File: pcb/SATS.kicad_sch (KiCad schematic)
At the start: 27 parts, among them J1 Raspberry_Pi_2_3, J10 EXT_GPIO, J11 EXT_GPIO, J12 EXT_GPIO, J13 EXT_GPIO, J2 A00-432-262-450, J3 AudioJack4_SwitchTR1, J4 5V, J5 3.3V, J6 Card LED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

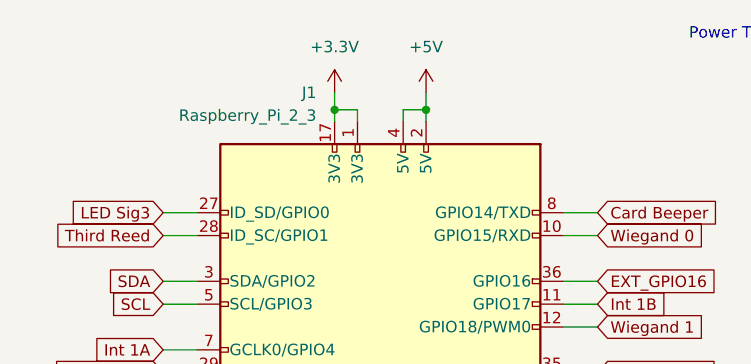
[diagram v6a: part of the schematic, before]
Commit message: Clean Board Edge and Foottprints
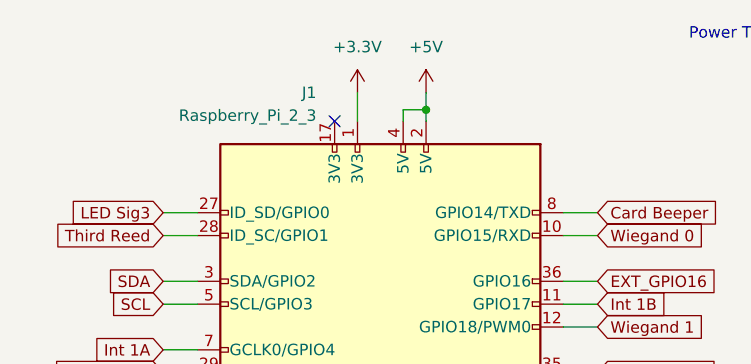
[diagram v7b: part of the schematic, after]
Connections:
- net +3V3: no longer J1.17 (3V3)
- no-connect marks 14 -> 15
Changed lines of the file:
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@@
   (junction (at 221.615 85.725) (diameter 0) (color 0 0 0 0)
   )
-  (junction (at 48.26 23.495) (diameter 0) (color 0 0 0 0)
-  )
   (junction (at 121.285 154.305) (diameter 0) (color 0 0 0 0)
   )
@@
   )
   (no_connect (at 271.78 64.77))
+  (no_connect (at 48.26 24.765))
   (no_connect (at 271.78 67.31))
   (no_connect (at 271.78 133.985))
@@
     (stroke (width 0) (type default) (color 0 0 0 0))
   )
-  (wire (pts (xy 48.26 21.59) (xy 48.26 23.495))
-    (stroke (width 0) (type default) (color 0 0 0 0))
-  )
   (wire (pts (xy 30.48 179.07) (xy 34.29 179.07))
     (stroke (width 0) (type default) (color 0 0 0 0))
@@
     (stroke (width 0) (type default) (color 0 0 0 0))
   )
-  (wire (pts (xy 48.26 23.495) (xy 50.8 23.495))
-    (stroke (width 0) (type default) (color 0 0 0 0))
-  )
   (wire (pts (xy 233.68 46.99) (xy 236.22 46.99))
     (stroke (width 0) (type default) (color 0 0 0 0))
@@
     (stroke (width 0) (type default) (color 0 0 0 0))
   )
-  (wire (pts (xy 48.26 23.495) (xy 48.26 24.765))
-    (stroke (width 0) (type default) (color 0 0 0 0))
-  )
-  (wire (pts (xy 50.8 23.495) (xy 50.8 24.765))
+  (wire (pts (xy 50.8 21.59) (xy 50.8 24.765))
     (stroke (width 0) (type default) (color 0 0 0 0))
   )
@@
     (pin "1")
   )
-  (symbol (lib_id "power:+3.3V") (at 48.26 21.59 0) (mirror y) (unit 1)
-    (in_bom yes) (on_board yes) (fields_autoplaced)
-    (property "Reference" "#PWR0121" (id 0) (at 48.26 25.4 0)
-      (effects (font (size 1.27 1.27)) hide)
-    )
-    (property "Value" "+3.3V" (id 1) (at 48.26 16.51 0))
-    (property "Footprint" "" (id 2) (at 48.26 21.59 0)
-      (effects (font (size 1.27 1.27)) hide)
-    )
-    (property "Datasheet" "" (id 3) (at 48.26 21.59 0)
-      (effects (font (size 1.27 1.27)) hide)
-    )
+  (symbol (lib_id "power:+3.3V") (at 50.8 21.59 0) (mirror y) (unit 1)
+    (in_bom yes) (on_board yes) (fields_autoplaced)
+    (property "Reference" "#PWR0121" (id 0) (at 50.8 25.4 0)
+      (effects (font (size 1.27 1.27)) hide)
+    )
+    (property "Value" "+3.3V" (id 1) (at 50.8 16.51 0))
+    (property "Footprint" "" (id 2) (at 50.8 21.59 0)
+      (effects (font (size 1.27 1.27)) hide)
+    )
+    (property "Datasheet" "" (id 3) (at 50.8 21.59 0)
+      (effects (font (size 1.27 1.27)) hide)
+    )

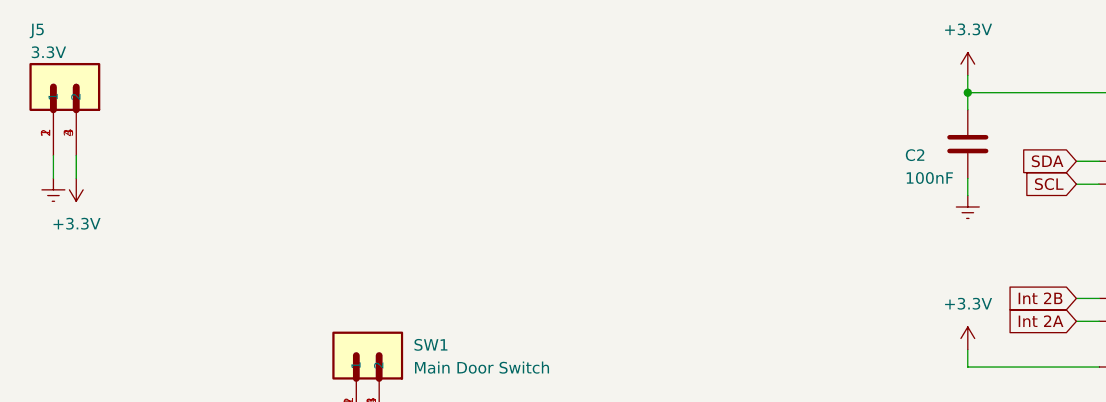
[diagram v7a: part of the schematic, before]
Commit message: Add Mounting Holes and Fix Errors
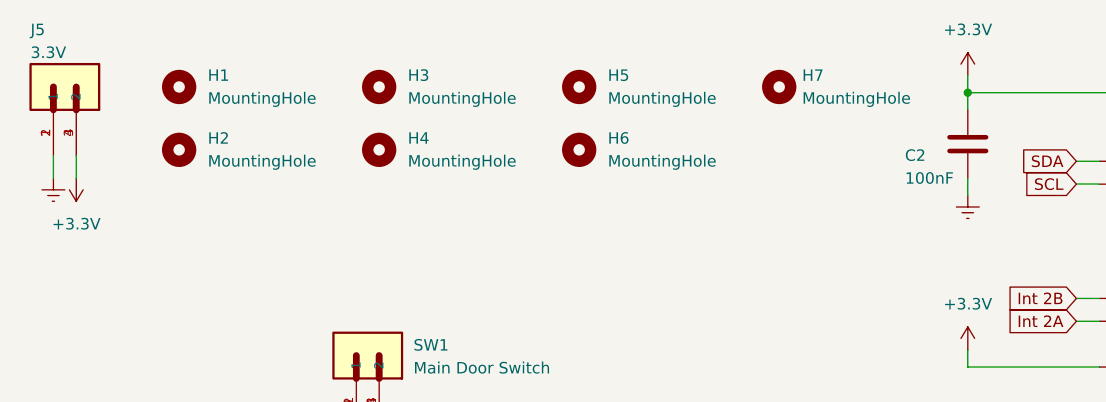
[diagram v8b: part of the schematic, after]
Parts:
- added H1, H2, H3, H4, H5, H6, H7: MountingHole, MountingHole:MountingHole_2.7mm_M2.5, symbol Mechanical:MountingHole
- U3: footprint CD40109BE:DIP794W45P254L1969H508Q16 -> Package_DIP:DIP-16_W7.62mm
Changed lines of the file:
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@@
     (pin "4")
+  )
+  (symbol (lib_id "Mechanical:MountingHole") (at 133.985 27.94 0) (unit 1)
+    (in_bom yes) (on_board yes) (fields_autoplaced)
+    (property "Reference" "H2" (id 0) (at 137.16 26.6699 0)
+      (effects (font (size 1.27 1.27)) (justify left))
+    )
+    (property "Value" "MountingHole" (id 1) (at 137.16 29.2099 0)
+      (effects (font (size 1.27 1.27)) (justify left))
+    )
+    (property "Footprint" "MountingHole:MountingHole_2.7mm_M2.5" (id 2) (at 133.985 27.94 0)
+      (effects (font (size 1.27 1.27)) hide)
+    )
+    (property "Datasheet" "~" (id 3) (at 133.985 27.94 0)
+      (effects (font (size 1.27 1.27)) hide)
+    )
   )
   (symbol (lib_id "TerminalConn:1862042") (at 41.91 104.14 0) (unit 1)
@@
     (pin "3")
     (pin "4")
+  )
+  (symbol (lib_id "Mechanical:MountingHole") (at 178.435 20.955 0) (unit 1)
+    (in_bom yes) (on_board yes) (fields_autoplaced)
+    (property "Reference" "H5" (id 0) (at 181.61 19.6849 0)
+      (effects (font (size 1.27 1.27)) (justify left))
+    )
+    (property "Value" "MountingHole" (id 1) (at 181.61 22.2249 0)
+      (effects (font (size 1.27 1.27)) (justify left))
+    )
+    (property "Footprint" "MountingHole:MountingHole_2.7mm_M2.5" (id 2) (at 178.435 20.955 0)
+      (effects (font (size 1.27 1.27)) hide)
+    )
+    (property "Datasheet" "~" (id 3) (at 178.435 20.955 0)
+      (effects (font (size 1.27 1.27)) hide)
+    )
   )
   (symbol (lib_id "CD40109BE:CD40109BE") (at 92.71 169.545 0) (unit 1)
@@
     (property "Reference" "U3" (id 0) (at 92.71 144.145 0))
     (property "Value" "CD40109BE" (id 1) (at 92.71 146.685 0))
-    (property "Footprint" "CD40109BE:DIP794W45P254L1969H508Q16" (id 2) (at 92.71 169.545 0)
+    (property "Footprint" "Package_DIP:DIP-16_W7.62mm" (id 2) (at 92.71 169.545 0)
       (effects (font (size 1.27 1.27)) (justify bottom) hide)
     )
@@
     (pin "8")
     (pin "9")
+  )
+  (symbol (lib_id "Mechanical:MountingHole") (at 178.435 27.94 0) (unit 1)
+    (in_bom yes) (on_board yes) (fields_autoplaced)
+    (property "Reference" "H6" (id 0) (at 181.61 26.6699 0)
+      (effects (font (size 1.27 1.27)) (justify left))
+    )
+    (property "Value" "MountingHole" (id 1) (at 181.61 29.2099 0)
+      (effects (font (size 1.27 1.27)) (justify left))
+    )
+    (property "Footprint" "MountingHole:MountingHole_2.7mm_M2.5" (id 2) (at 178.435 27.94 0)
+      (effects (font (size 1.27 1.27)) hide)
+    )
+    (property "Datasheet" "~" (id 3) (at 178.435 27.94 0)
+      (effects (font (size 1.27 1.27)) hide)
+    )
   )
   (symbol (lib_id "Interface_Expansion:MCP23017_SP") (at 254 113.665 0) (unit 1)
@@
     (pin "1")
   )
+  (symbol (lib_id "Mechanical:MountingHole") (at 200.66 20.955 0) (unit 1)
+    (in_bom yes) (on_board yes) (fields_autoplaced)
+    (property "Reference" "H7" (id 0) (at 203.2 19.6849 0)
+      (effects (font (size 1.27 1.27)) (justify left))
+    )
+    (property "Value" "MountingHole" (id 1) (at 203.2 22.2249 0)
+      (effects (font (size 1.27 1.27)) (justify left))
+    )
+    (property "Footprint" "MountingHole:MountingHole_2.7mm_M2.5" (id 2) (at 200.66 20.955 0)
+      (effects (font (size 1.27 1.27)) hide)
+    )
+    (property "Datasheet" "~" (id 3) (at 200.66 20.955 0)
+      (effects (font (size 1.27 1.27)) hide)
+    )
+  )
   (symbol (lib_id "power:Earth") (at 221.615 33.02 0) (unit 1)
     (in_bom yes) (on_board yes) (fields_autoplaced)
@@
     (pin "1")
   )
+  (symbol (lib_id "Mechanical:MountingHole") (at 156.21 27.94 0) (unit 1)
+    (in_bom yes) (on_board yes)
+    (property "Reference" "H4" (id 0) (at 159.385 26.67 0)
+      (effects (font (size 1.27 1.27)) (justify left))
+    )
+    (property "Value" "MountingHole" (id 1) (at 159.385 29.21 0)
+      (effects (font (size 1.27 1.27)) (justify left))
+    )
+    (property "Footprint" "MountingHole:MountingHole_2.7mm_M2.5" (id 2) (at 156.21 27.94 0)
+      (effects (font (size 1.27 1.27)) hide)
+    )
+    (property "Datasheet" "~" (id 3) (at 156.21 27.94 0)
+      (effects (font (size 1.27 1.27)) hide)
+    )
+  )
   (symbol (lib_id "power:Earth") (at 233.68 135.89 0) (unit 1)
     (in_bom yes) (on_board yes) (fields_autoplaced)
@@
     (pin "1")
   )
+  (symbol (lib_id "Mechanical:MountingHole") (at 133.985 20.955 0) (unit 1)
+    (in_bom yes) (on_board yes) (fields_autoplaced)
+    (property "Reference" "H1" (id 0) (at 137.16 19.6849 0)
+      (effects (font (size 1.27 1.27)) (justify left))
+    )
+    (property "Value" "MountingHole" (id 1) (at 137.16 22.2249 0)
+      (effects (font (size 1.27 1.27)) (justify left))
+    )
+    (property "Footprint" "MountingHole:MountingHole_2.7mm_M2.5" (id 2) (at 133.985 20.955 0)
+      (effects (font (size 1.27 1.27)) hide)
+    )
+    (property "Datasheet" "~" (id 3) (at 133.985 20.955 0)
+      (effects (font (size 1.27 1.27)) hide)
+    )
+  )
   (symbol (lib_id "power:+5V") (at 77.47 90.17 0) (unit 1)
     (in_bom yes) (on_board yes) (fields_autoplaced)
@@
     (pin "3")
     (pin "4")
+  )
+  (symbol (lib_id "Mechanical:MountingHole") (at 156.21 20.955 0) (unit 1)
+    (in_bom yes) (on_board yes)
+    (property "Reference" "H3" (id 0) (at 159.385 19.685 0)
+      (effects (font (size 1.27 1.27)) (justify left))
+    )
+    (property "Value" "MountingHole" (id 1) (at 159.385 22.225 0)
+      (effects (font (size 1.27 1.27)) (justify left))
+    )
+    (property "Footprint" "MountingHole:MountingHole_2.7mm_M2.5" (id 2) (at 156.21 20.955 0)
+      (effects (font (size 1.27 1.27)) hide)
+    )
+    (property "Datasheet" "~" (id 3) (at 156.21 20.955 0)
+      (effects (font (size 1.27 1.27)) hide)
+    )
   )
   (symbol (lib_id "Device:C") (at 134.62 158.115 0) (unit 1)
@@
       (reference "D1") (unit 1) (value "1N4007") (footprint "Diode_THT:D_DO-41_SOD81_P10.16mm_Horizontal")
     )
+    (path "/c6a9bc83-ca74-4ca1-a41e-ea571fe21c97"
+      (reference "H1") (unit 1) (value "MountingHole") (footprint "MountingHole:MountingHole_2.7mm_M2.5")
+    )
+    (path "/1b09e8af-b104-4bf4-88b1-ae5d3b5fbb54"
+      (reference "H2") (unit 1) (value "MountingHole") (footprint "MountingHole:MountingHole_2.7mm_M2.5")
+    )
+    (path "/da24104e-b23d-42c4-adcf-7a52acbdfe85"
+      (reference "H3") (unit 1) (value "MountingHole") (footprint "MountingHole:MountingHole_2.7mm_M2.5")
+    )
+    (path "/b7b125ac-9c68-46ee-8452-5104b7808750"
+      (reference "H4") (unit 1) (value "MountingHole") (footprint "MountingHole:MountingHole_2.7mm_M2.5")
+    )
+    (path "/1e70d3ac-52b6-4df7-9166-b61dc9d23c7b"
+      (reference "H5") (unit 1) (value "MountingHole") (footprint "MountingHole:MountingHole_2.7mm_M2.5")
+    )
+    (path "/23537ee2-e0a9-4436-82e1-1c41878bdf24"
+      (reference "H6") (unit 1) (value "MountingHole") (footprint "MountingHole:MountingHole_2.7mm_M2.5")
+    )
+    (path "/6396cd5b-2c5c-4a84-b28a-279d82b2080a"
+      (reference "H7") (unit 1) (value "MountingHole") (footprint "MountingHole:MountingHole_2.7mm_M2.5")
+    )
     (path "/422a914e-8b99-4ff0-8ddf-1d6a3d23d7a7"
       (reference "J1") (unit 1) (value "Raspberry_Pi_2_3") (footprint "Connector_PinSocket_2.54mm:PinSocket_2x20_P2.54mm_Vertical")
@@
     )
     (path "/201bf6e5-0ee1-4b89-8a4a-ce5cd24fad2f"
-      (reference "U3") (unit 1) (value "CD40109BE") (footprint "CD40109BE:DIP794W45P254L1969H508Q16")
+      (reference "U3") (unit 1) (value "CD40109BE") (footprint "Package_DIP:DIP-16_W7.62mm")
     )
     (path "/895ab77c-6b59-440a-8f64-961029be5e6e"
